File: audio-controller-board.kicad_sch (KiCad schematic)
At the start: 4 parts

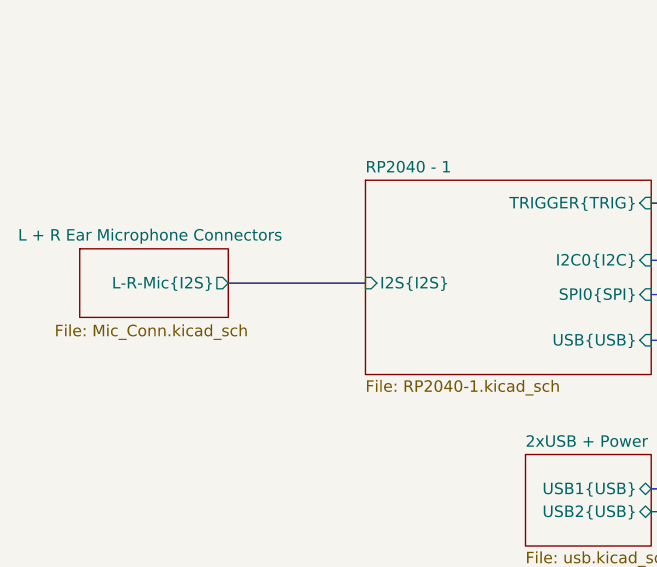
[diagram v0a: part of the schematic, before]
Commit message: [#71230] Add support for PDM microphone
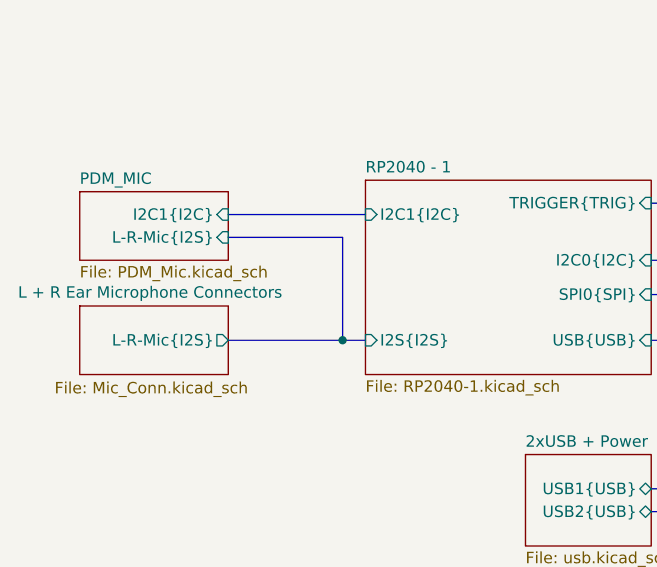
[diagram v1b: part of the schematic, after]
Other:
- added sheet PDM_MIC (PDM_Mic.kicad_sch)
- sheet RP2040 - 1 ports: added I2C1{I2C}; removed none
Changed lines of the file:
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@@
 		(members "TRIG1" "TRIG2" "TRIG3" "TRIG4")
 	)
+	(junction
+		(at 148.59 138.43)
+		(diameter 0)
+		(color 0 0 0 0)
+	)
+	(bus
+		(pts
+			(xy 135.89 124.46) (xy 151.13 124.46)
+		)
+		(stroke
+			(width 0)
+			(type default)
+		)
+	)
 	(bus
 		(pts
@@
 	(bus
 		(pts
-			(xy 135.89 132.08) (xy 151.13 132.08)
+			(xy 190.5 154.94) (xy 190.5 138.43)
+		)
+		(stroke
+			(width 0)
+			(type default)
+		)
+	)
+	(bus
+		(pts
+			(xy 182.88 157.48) (xy 194.31 157.48)
+		)
+		(stroke
+			(width 0)
+			(type default)
+		)
+	)
+	(bus
+		(pts
+			(xy 194.31 106.68) (xy 201.93 106.68)
+		)
+		(stroke
+			(width 0)
+			(type default)
+		)
+	)
+	(bus
+		(pts
+			(xy 182.88 154.94) (xy 190.5 154.94)
+		)
+		(stroke
+			(width 0)
+			(type default)
+		)
+	)
+	(bus
+		(pts
+			(xy 182.88 123.19) (xy 190.5 123.19)
+		)
+		(stroke
+			(width 0)
+			(type default)
+		)
+	)
+	(bus
+		(pts
+			(xy 148.59 138.43) (xy 151.13 138.43)
 		)
 		(stroke
@@
 	(bus
 		(pts
-			(xy 190.5 154.94) (xy 190.5 138.43)
-		)
-		(stroke
-			(width 0)
-			(type default)
-		)
-	)
-	(bus
-		(pts
-			(xy 182.88 157.48) (xy 194.31 157.48)
-		)
-		(stroke
-			(width 0)
-			(type default)
-		)
-	)
-	(bus
-		(pts
-			(xy 194.31 106.68) (xy 201.93 106.68)
-		)
-		(stroke
-			(width 0)
-			(type default)
-		)
-	)
-	(bus
-		(pts
-			(xy 182.88 154.94) (xy 190.5 154.94)
-		)
-		(stroke
-			(width 0)
-			(type default)
-		)
-	)
-	(bus
-		(pts
-			(xy 182.88 123.19) (xy 190.5 123.19)
+			(xy 135.89 127) (xy 148.59 127)
 		)
 		(stroke
@@
 	(bus
 		(pts
+			(xy 135.89 138.43) (xy 148.59 138.43)
+		)
+		(stroke
+			(width 0)
+			(type default)
+			(color 241 95 50 1)
+		)
+	)
+	(bus
+		(pts
 			(xy 182.88 133.35) (xy 200.66 133.35)
 		)
@@
 		(pts
 			(xy 190.5 138.43) (xy 182.88 138.43)
+		)
+		(stroke
+			(width 0)
+			(type default)
+		)
+	)
+	(bus
+		(pts
+			(xy 148.59 127) (xy 148.59 138.43)
 		)
 		(stroke
@@
 		)
 		(pin "I2S{I2S}" input
-			(at 151.13 132.08 180)
+			(at 151.13 138.43 180)
 			(effects
 				(font
@@
 				)
 				(justify right)
+			)
+		)
+		(pin "I2C1{I2C}" input
+			(at 151.13 124.46 180)
+			(effects
+				(font
+					(size 1.27 1.27)
+				)
+				(justify left)
 			)
 		)
@@
 	)
 	(sheet
+		(at 119.38 121.92)
+		(size 16.51 7.62)
+		(fields_autoplaced yes)
+		(stroke
+			(width 0.1524)
+			(type solid)
+		)
+		(fill
+			(color 0 0 0 0.0000)
+		)
+		(property "Sheetname" "PDM_MIC"
+			(at 119.38 121.2084 0)
+			(effects
+				(font
+					(size 1.27 1.27)
+				)
+				(justify left bottom)
+			)
+		)
+		(property "Sheetfile" "PDM_Mic.kicad_sch"
+			(at 119.38 130.1246 0)
+			(effects
+				(font
+					(size 1.27 1.27)
+				)
+				(justify left top)
+			)
+		)
+		(pin "L-R-Mic{I2S}" input
+			(at 135.89 127 0)
+			(effects
+				(font
+					(size 1.27 1.27)
+				)
+				(justify right)
+			)
+		)
+		(pin "I2C1{I2C}" input
+			(at 135.89 124.46 0)
+			(effects
+				(font
+					(size 1.27 1.27)
+				)
+				(justify right)
+			)
+		)
+		(instances
+			(project "audio-controller-board"
+				(path "/7fb12ebf-f685-4412-b638-445b1bf344bc"
+					(page "8")
+				)
+			)
+		)
+	)
+	(sheet
 		(at 168.91 151.13)
 		(size 13.97 10.16)
@@
 	)
 	(sheet
-		(at 119.38 128.27)
+		(at 119.38 134.62)
 		(size 16.51 7.62)
 		(stroke
@@
 		)
 		(property "Sheetname" "L + R Ear Microphone Connectors"
-			(at 112.522 127.508 0)
+			(at 112.522 133.858 0)
 			(effects
 				(font
@@
 		)
 		(property "Sheetfile" "Mic_Conn.kicad_sch"
-			(at 116.586 136.652 0)
+			(at 116.586 143.002 0)
 			(effects
 				(font
@@
 		)
 		(pin "L-R-Mic{I2S}" output
-			(at 135.89 132.08 0)
-			(effects
-				(font
+			(at 135.89 138.43 0)
+			(effects
+				(font

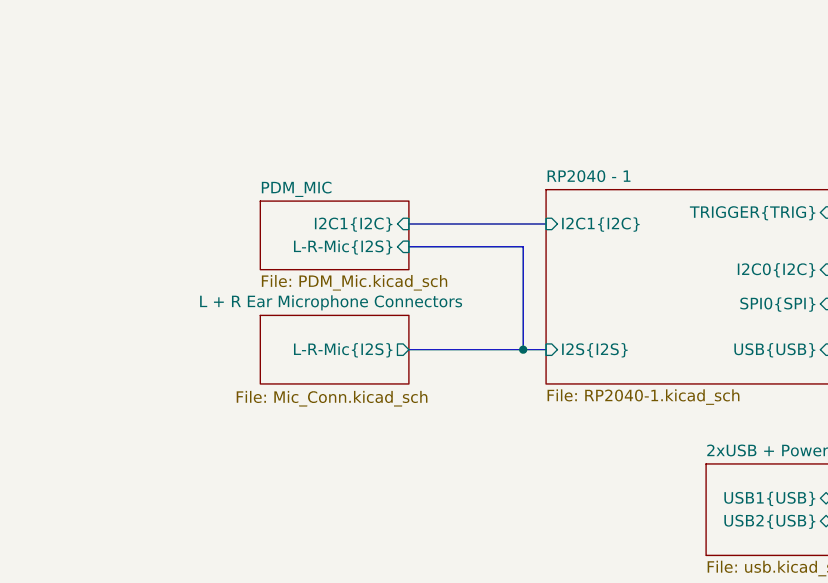
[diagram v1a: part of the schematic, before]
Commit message: [#71230] Add option to connect PDM mic directly to RP2040-0
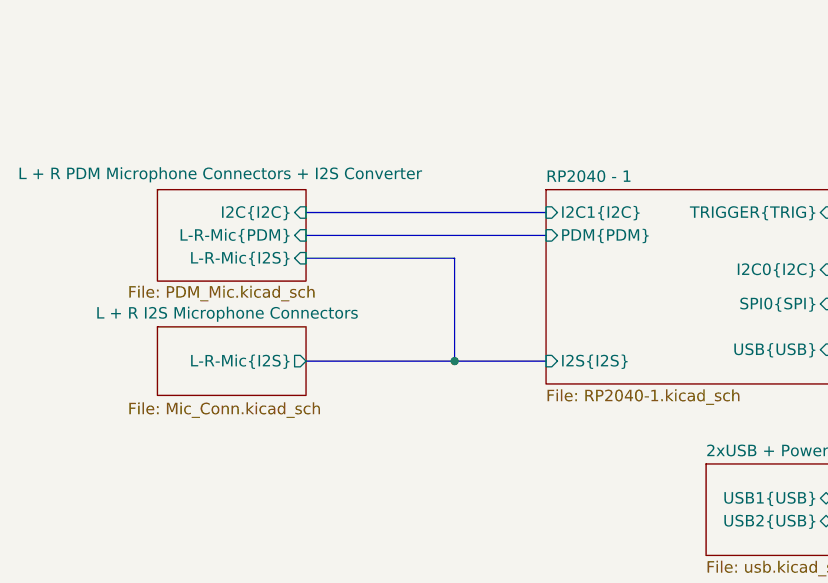
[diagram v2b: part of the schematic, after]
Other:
- sheet L + R Ear Microphone Connectors renamed L + R I2S Microphone Connectors
- sheet PDM_MIC renamed L + R PDM Microphone Connectors + I2S Converter
- sheet L + R PDM Microphone Connectors + I2S Converter ports: added I2C{I2C}, L-R-Mic{PDM}; removed I2C1{I2C}
- sheet RP2040 - 1 ports: added PDM{PDM}; removed none
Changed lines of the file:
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@@
 		(members "SD" "SCK" "WS")
+	)
+	(bus_alias "PDM"
+		(members "DATA" "CLOCK")
 	)
 	(bus_alias "SPI"
@@
 	)
 	(junction
-		(at 148.59 138.43)
+		(at 140.97 139.7)
 		(diameter 0)
 		(color 0 0 0 0)
@@
 	(bus
 		(pts
-			(xy 135.89 124.46) (xy 151.13 124.46)
+			(xy 124.46 125.73) (xy 151.13 125.73)
+		)
+		(stroke
+			(width 0)
+			(type default)
+		)
+	)
+	(bus
+		(pts
+			(xy 124.46 123.19) (xy 151.13 123.19)
 		)
 		(stroke
@@
 	(bus
 		(pts
+			(xy 140.97 139.7) (xy 151.13 139.7)
+		)
+		(stroke
+			(width 0)
+			(type default)
+			(color 241 95 50 1)
+		)
+	)
+	(bus
+		(pts
 			(xy 182.88 154.94) (xy 190.5 154.94)
 		)
@@
 	(bus
 		(pts
-			(xy 148.59 138.43) (xy 151.13 138.43)
+			(xy 124.46 128.27) (xy 140.97 128.27)
 		)
 		(stroke
@@
 	(bus
 		(pts
-			(xy 135.89 127) (xy 148.59 127)
-		)
-		(stroke
-			(width 0)
-			(type default)
-		)
-	)
-	(bus
-		(pts
 			(xy 194.31 123.19) (xy 200.66 123.19)
 		)
@@
 	(bus
 		(pts
-			(xy 135.89 138.43) (xy 148.59 138.43)
+			(xy 124.46 139.7) (xy 140.97 139.7)
 		)
 		(stroke
@@
 	(bus
 		(pts
-			(xy 148.59 127) (xy 148.59 138.43)
-		)
-		(stroke
-			(width 0)
-			(type default)
+			(xy 140.97 128.27) (xy 140.97 139.7)
+		)
+		(stroke
+			(width 0)
+			(type default)
+			(color 241 95 50 1)
 		)
 	)
@@
 		)
 		(pin "I2S{I2S}" input
-			(at 151.13 138.43 180)
+			(at 151.13 139.7 180)
 			(effects
 				(font
@@
 		)
 		(pin "I2C1{I2C}" input
-			(at 151.13 124.46 180)
+			(at 151.13 123.19 180)
+			(effects
+				(font
+					(size 1.27 1.27)
+				)
+				(justify left)
+			)
+		)
+		(pin "PDM{PDM}" input
+			(at 151.13 125.73 180)
 			(effects
 				(font
@@
 	)
 	(sheet
-		(at 119.38 121.92)
-		(size 16.51 7.62)
-		(fields_autoplaced yes)
+		(at 107.95 120.65)
+		(size 16.51 10.16)
 		(stroke
 			(width 0.1524)
@@
 			(color 0 0 0 0.0000)
 		)
-		(property "Sheetname" "PDM_MIC"
-			(at 119.38 121.2084 0)
+		(property "Sheetname" "L + R PDM Microphone Connectors + I2S Converter"
+			(at 92.456 119.634 0)
 			(effects
 				(font
@@
 		)
 		(property "Sheetfile" "PDM_Mic.kicad_sch"
-			(at 119.38 130.1246 0)
+			(at 104.648 131.318 0)
 			(effects
 				(font
@@
 		)
 		(pin "L-R-Mic{I2S}" input
-			(at 135.89 127 0)
+			(at 124.46 128.27 0)
 			(effects
 				(font
@@
 			)
 		)
-		(pin "I2C1{I2C}" input
-			(at 135.89 124.46 0)
+		(pin "I2C{I2C}" input
+			(at 124.46 123.19 0)
+			(effects
+				(font
+					(size 1.27 1.27)
+				)
+				(justify right)
+			)
+		)
+		(pin "L-R-Mic{PDM}" input
+			(at 124.46 125.73 0)
 			(effects
 				(font
@@
 	)
 	(sheet
-		(at 119.38 134.62)
+		(at 107.95 135.89)
 		(size 16.51 7.62)
 		(stroke
@@
 			(color 0 0 0 0.0000)
 		)
-		(property "Sheetname" "L + R Ear Microphone Connectors"
-			(at 112.522 133.858 0)
+		(property "Sheetname" "L + R I2S Microphone Connectors"
+			(at 101.092 135.128 0)
 			(effects
 				(font
@@
 		)
 		(property "Sheetfile" "Mic_Conn.kicad_sch"
-			(at 116.586 143.002 0)
+			(at 104.648 144.272 0)
 			(effects
 				(font
@@
 		)
 		(pin "L-R-Mic{I2S}" output
-			(at 135.89 138.43 0)
-			(effects
-				(font
+			(at 124.46 139.7 0)
+			(effects
+				(font
